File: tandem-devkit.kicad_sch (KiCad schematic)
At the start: 20 parts, among them J101 Conn_01x02, J102 QWIIC I2C Connector

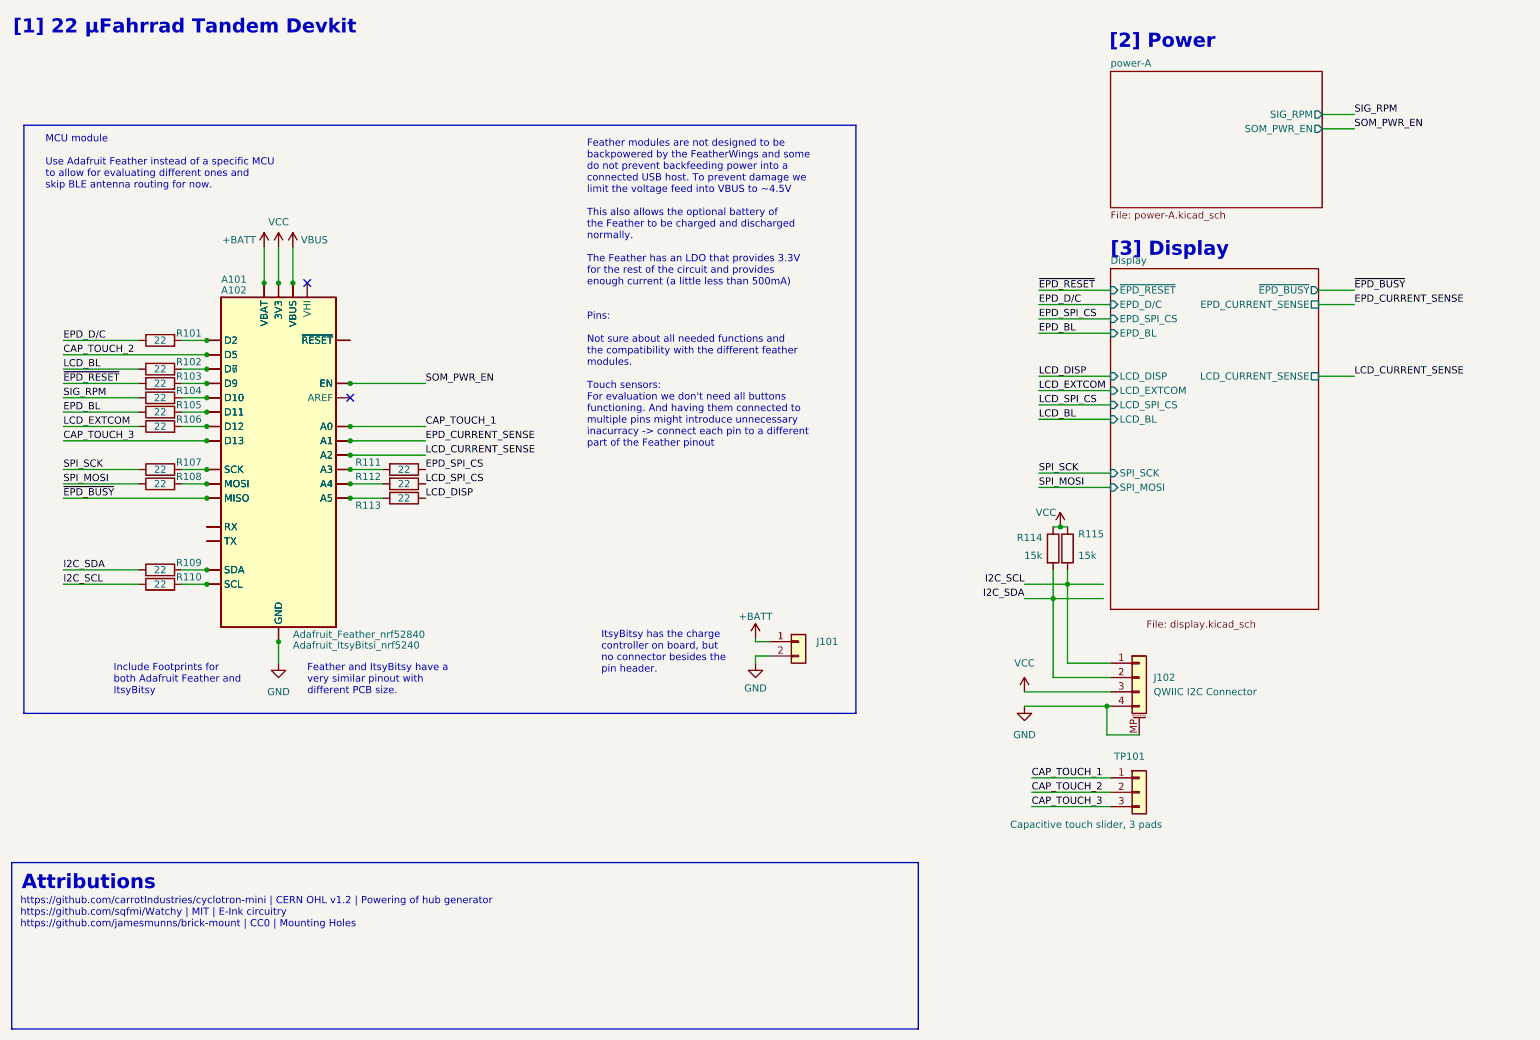
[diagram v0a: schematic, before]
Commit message: schematic: add another capacitive touch point, reorder feather pins
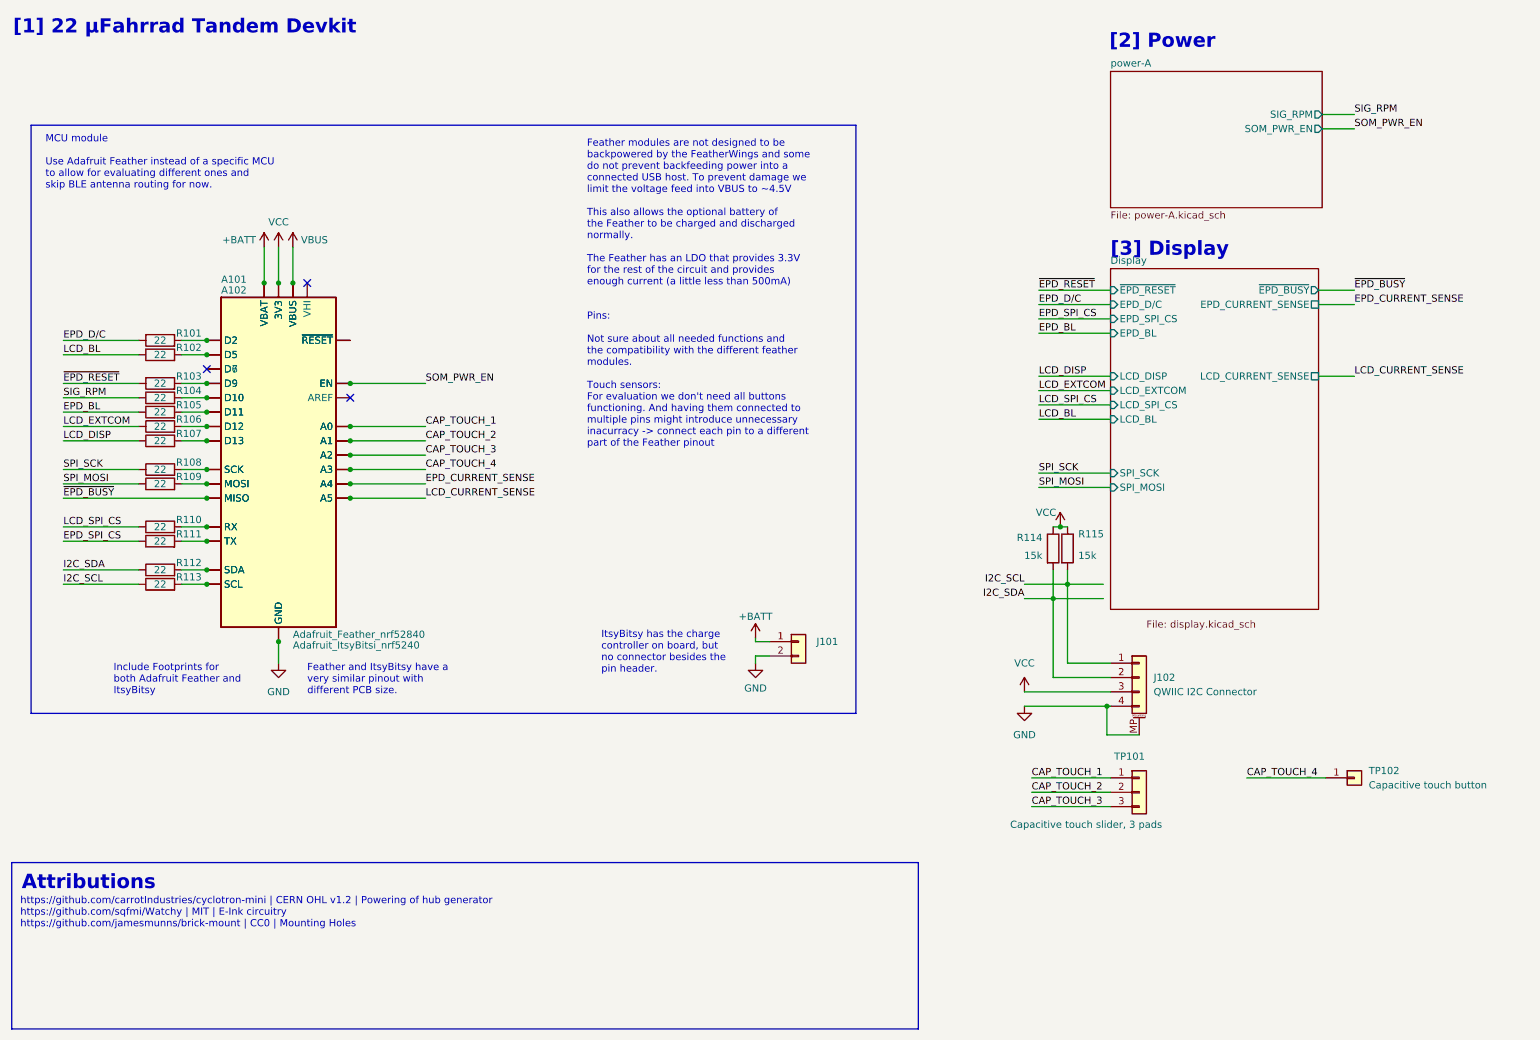
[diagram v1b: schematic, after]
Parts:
- added TP102: Capacitive touch button, symbol Connector_Generic:Conn_01x01
- renumbered R113 to R107, R107 to R108, R108 to R109, R112 to R110, R109 to R112, R110 to R113
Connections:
- net CAP_TOUCH_2: now also A101.6 (A1), A102.6 (A1); no longer A101.19 (D5), A102.19 (D5)
- net CAP_TOUCH_3: now also A101.7 (A2), A102.7 (A2); no longer A101.25 (D13), A102.25 (D13)
- net EPD_CURRENT_SENSE: now also A101.9 (A4), A102.9 (A4); no longer A101.6 (A1), A102.6 (A1)
- net LCD_CURRENT_SENSE: now also A101.10 (A5), A102.10 (A5); no longer A101.7 (A2), A102.7 (A2)
- net at A101.15 (RX), A102.14 (RX): now also R110.2
- net at A101.16 (TX), A102.15 (TX): now also R111.2
- net at A101.20 (D7), A102.20 (D6): no longer R102.2
- net CAP_TOUCH_4: now reaches A101.8 (A3), A102.8 (A3)
- net CAP_TOUCH_4: now also TP102.1 (Pin_1); no longer R111.2
- new net: A101.19 (D5), A102.19 (D5), R102.2
- new net: A101.25 (D13), A102.25 (D13), R107.2
- no-connect marks 2 -> 3
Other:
- moved on the sheet: R102, R107, R110, R111

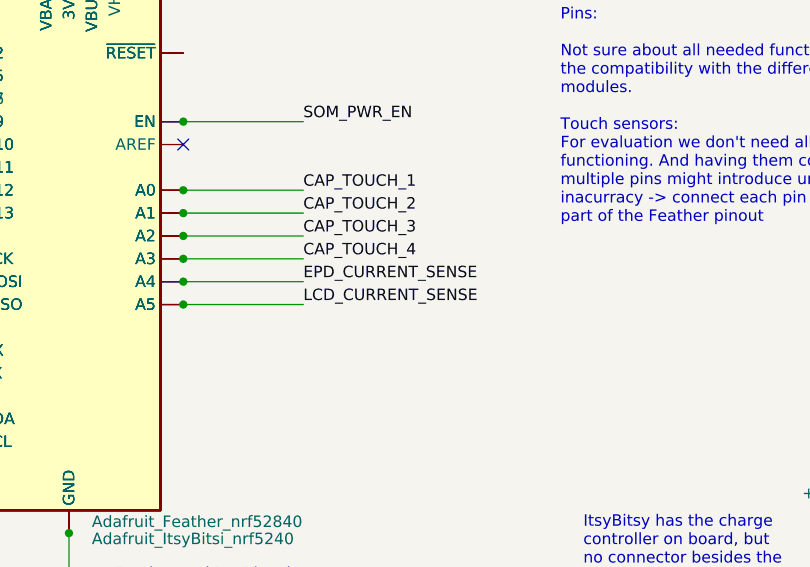
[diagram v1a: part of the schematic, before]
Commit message: schematic: switch EPD/LCD current sense lines to ease routing
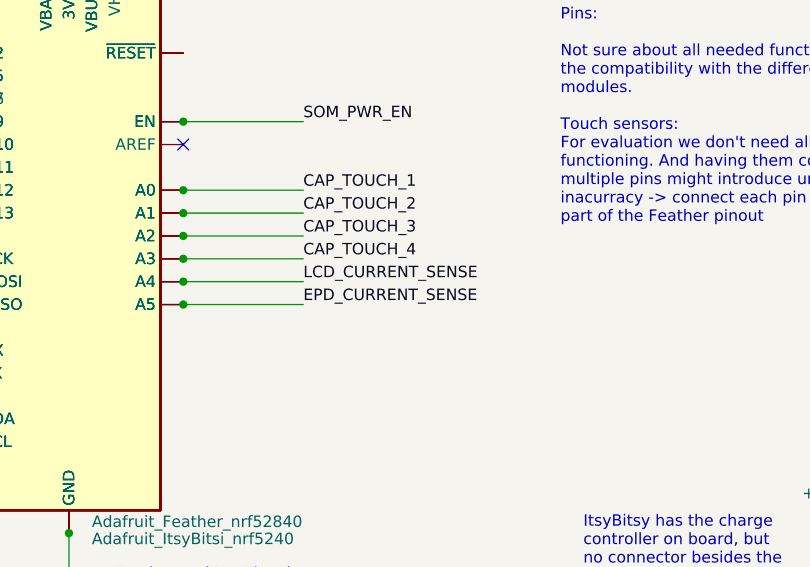
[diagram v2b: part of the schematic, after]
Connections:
- net EPD_CURRENT_SENSE: now also A101.10 (A5), A102.10 (A5); no longer A101.9 (A4), A102.9 (A4)
- net LCD_CURRENT_SENSE: now also A101.9 (A4), A102.9 (A4); no longer A101.10 (A5), A102.10 (A5)
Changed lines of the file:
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@@
     (effects (font (size 1.27 1.27)) (justify left bottom))
   )
-  (label "EPD_CURRENT_SENSE" (at 86.995 99.06 0)
+  (label "EPD_CURRENT_SENSE" (at 86.995 101.6 0)
     (effects (font (size 1.27 1.27)) (justify left bottom))
   )
@@
     (effects (font (size 1.27 1.27)) (justify left bottom))
   )
-  (label "LCD_CURRENT_SENSE" (at 86.995 101.6 0)
+  (label "LCD_CURRENT_SENSE" (at 86.995 99.06 0)
     (effects (font (size 1.27 1.27)) (justify left bottom))
   )

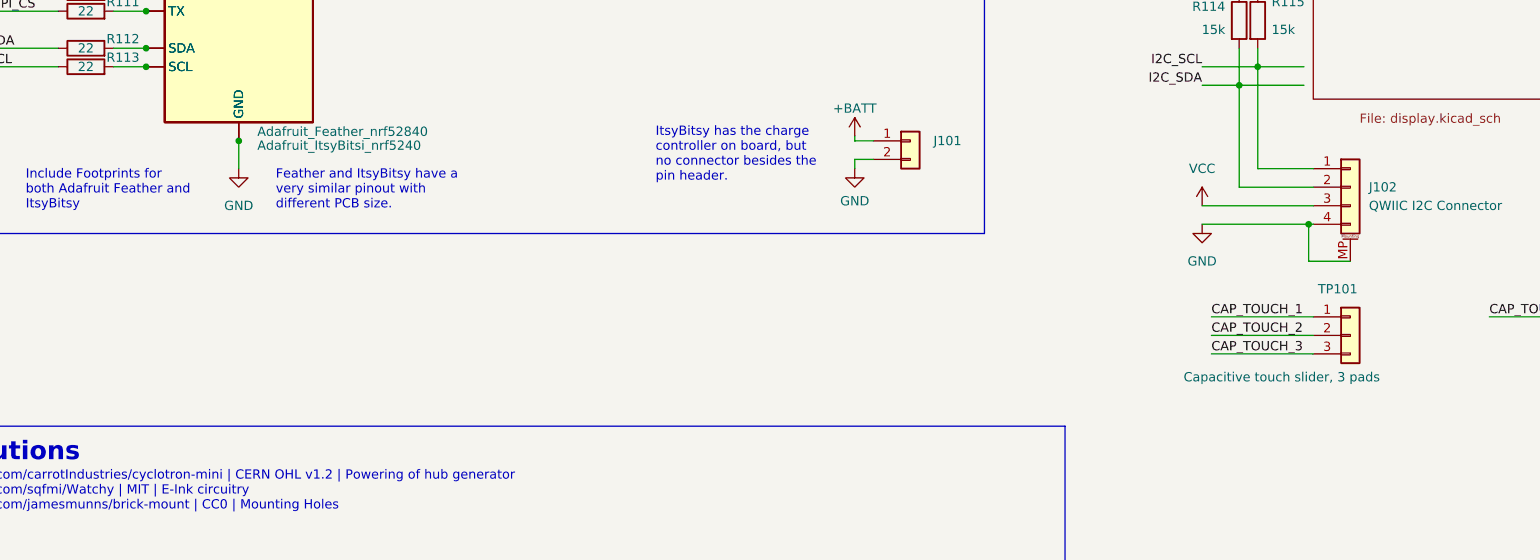
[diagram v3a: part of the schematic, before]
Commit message: Exchange brick-mount holes with actual footprint, connect holes to gnd
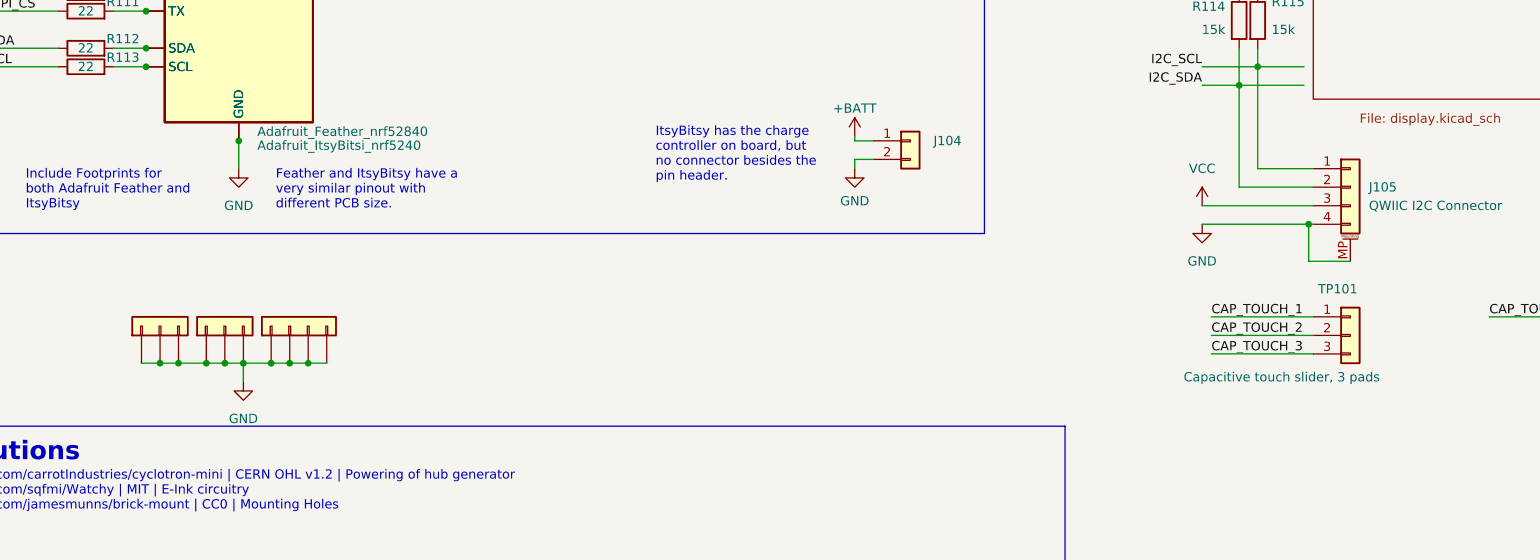
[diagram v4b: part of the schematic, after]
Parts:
- added J101, J102: Conn_01x03, brick-mount:brick-1x3, symbol Connector_Generic:Conn_01x03
- added J103: Conn_01x04, brick-mount:brick-1x4, symbol Connector_Generic:Conn_01x04
- renumbered J101 to J104, J102 to J105
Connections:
- net GND: now also J101.1 (Pin_1), J101.2 (Pin_2), J101.3 (Pin_3), J102.1 (Pin_1), J102.2 (Pin_2), J102.3 (Pin_3), J103.1 (Pin_1), J103.2 (Pin_2), J103.3 (Pin_3), J103.4 (Pin_4)

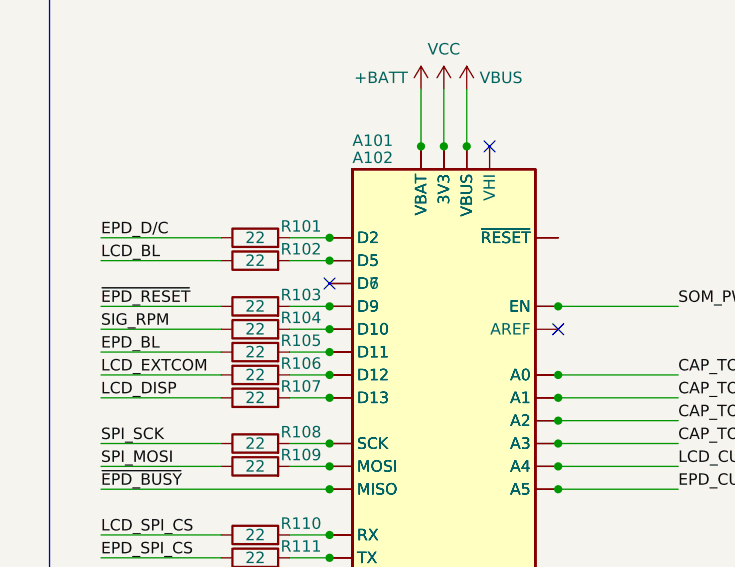
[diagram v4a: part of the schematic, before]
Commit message: connect everything except the capacitive touch sensors
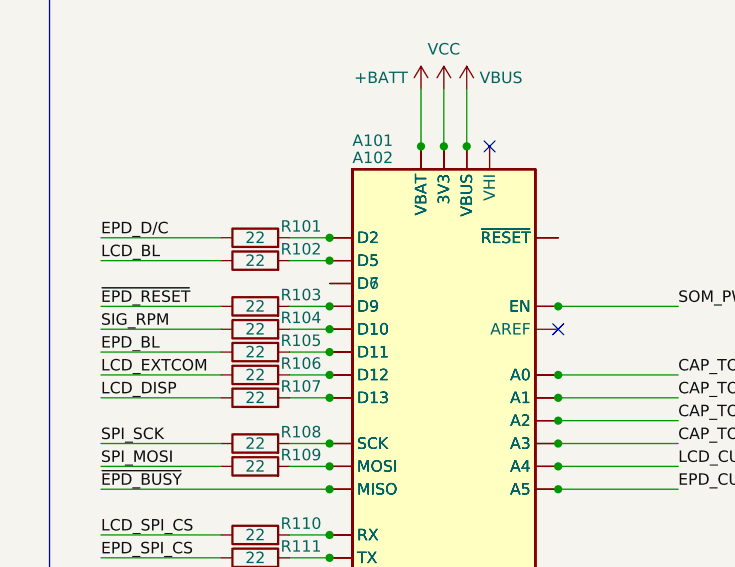
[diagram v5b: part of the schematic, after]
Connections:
- no-connect marks 3 -> 2
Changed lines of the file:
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@@
   (junction (at 48.26 109.22) (diameter 0) (color 0 0 0 0)
   )
-  (no_connect (at 48.26 78.74))
   (no_connect (at 73.66 83.82))
   (no_connect (at 66.04 63.5))
@@
   (symbol (lib_id "power:GND") (at 61.595 160.02 0) (unit 1)
     (in_bom yes) (on_board yes) (fields_autoplaced)
-    (property "Reference" "#PWR?" (id 0) (at 61.595 166.37 0)
+    (property "Reference" "#PWR0110" (id 0) (at 61.595 166.37 0)
       (effects (font (size 1.27 1.27)) hide)
     )
@@
       (reference "#PWR0109") (unit 1) (value "VCC") (footprint "")
     )
+    (path "/5609672f-1e6a-48cf-a156-8d669026c5a0"
+      (reference "#PWR0110") (unit 1) (value "GND") (footprint "")
+    )
     (path "/d5fdcc1b-217f-4399-86f5-956578dadb93/fa0616dd-983c-46a3-85e8-1186c07f2350"
       (reference "#PWR0201") (unit 1) (value "GNDPWR") (footprint "")
@@
       (reference "#PWR0313") (unit 1) (value "VCC") (footprint "")
     )
-    (path "/5609672f-1e6a-48cf-a156-8d669026c5a0"
-      (reference "#PWR?") (unit 1) (value "GND") (footprint "")
-    )
     (path "/112dc4b6-2daf-4c2e-96c0-b9ba5d7485bd"
